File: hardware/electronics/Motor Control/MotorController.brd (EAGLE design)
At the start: 58.4 x 53.3 mm, 10 parts, among them J1 AVR_SPI_PRG_6PTH, U1 ARDUINOR3-BPLACE, U2 ATMEGA328P_TQFP, U3 V_REG_317SMD, X1 HEADER_POS3_70555

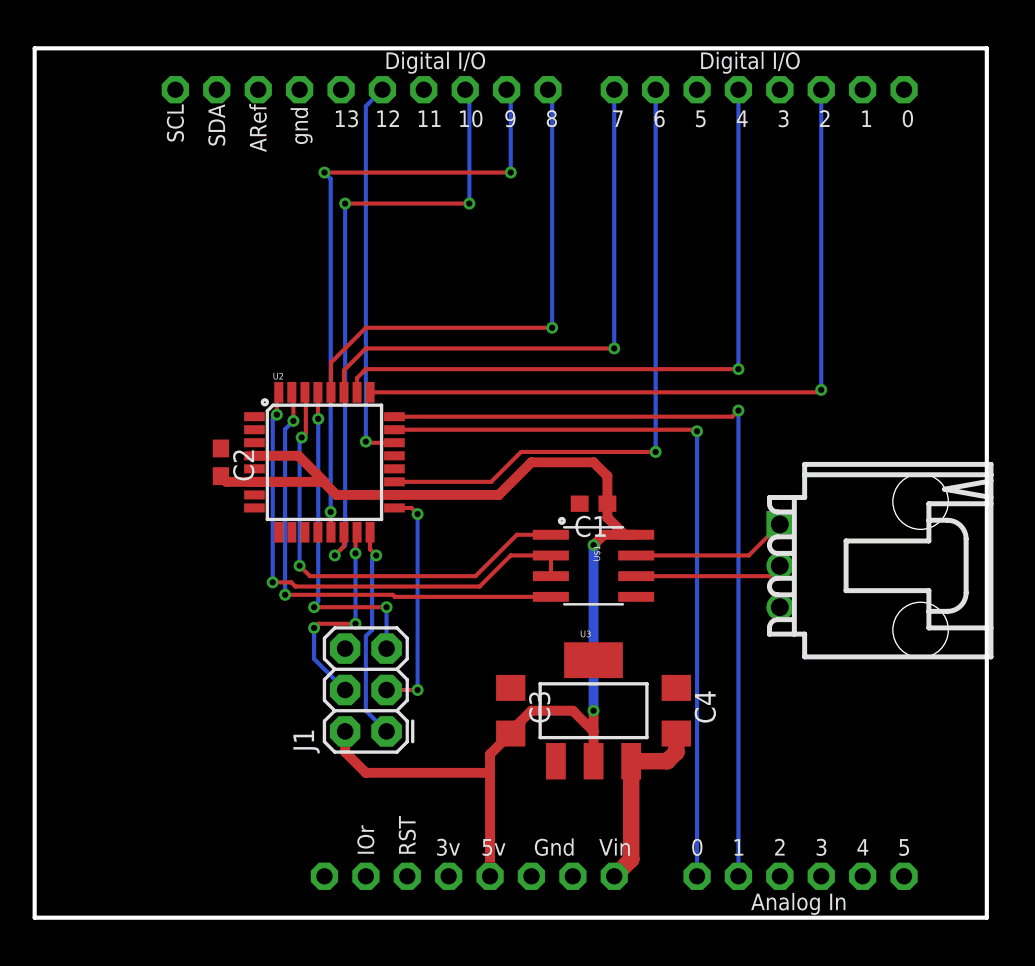
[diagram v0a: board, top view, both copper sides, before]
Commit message: Making sure we have the latest board in github
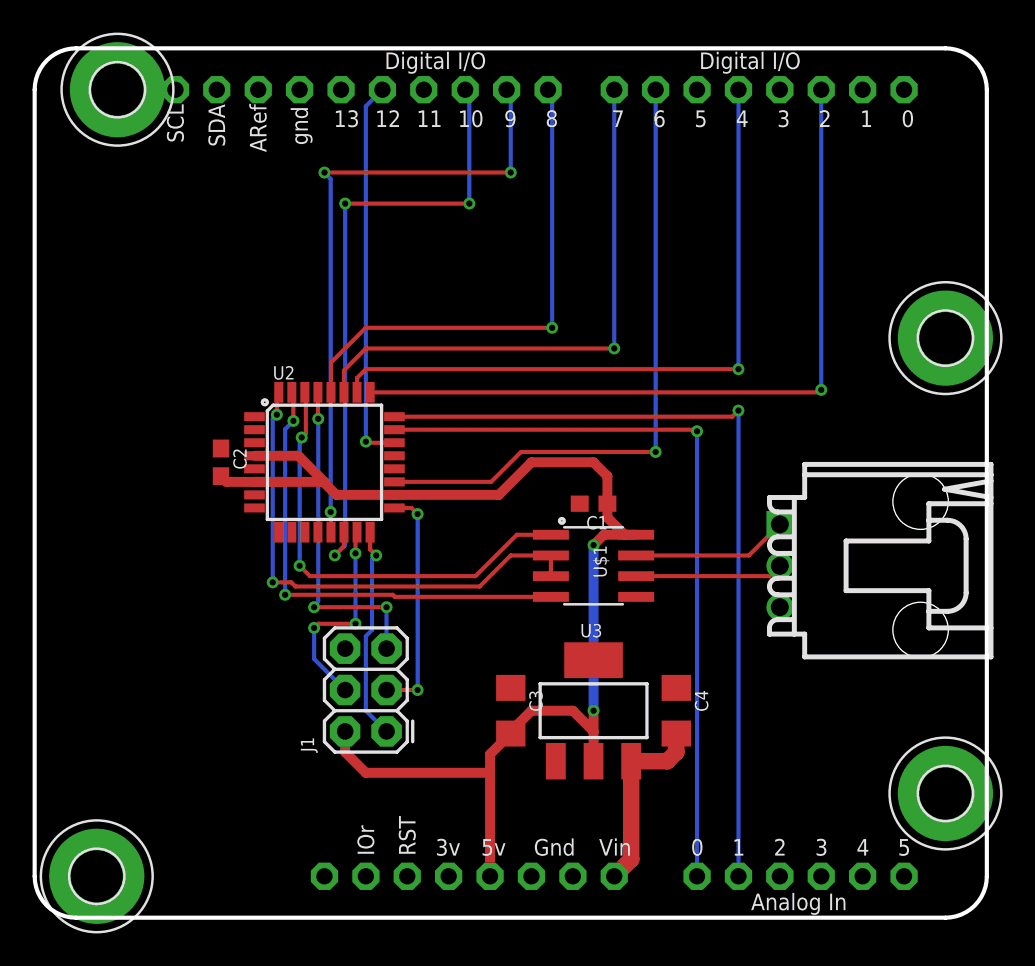
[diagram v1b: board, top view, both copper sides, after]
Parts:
- added H1, H2, H3, H4: MOUNT-PAD-ROUND3.2, holes:3,2-PAD
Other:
- outline, holes or cut-outs redrawn
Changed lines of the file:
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@@
 <board>
 <plain>
-<wire x1="0" y1="0" x2="58.42" y2="0" width="0.254" layer="20"/>
-<wire x1="58.42" y1="0" x2="58.42" y2="53.34" width="0.254" layer="20"/>
-<wire x1="58.42" y1="53.34" x2="0" y2="53.34" width="0.254" layer="20"/>
-<wire x1="0" y1="53.34" x2="0" y2="0" width="0.254" layer="20"/>
+<wire x1="0" y1="50.8" x2="0" y2="2.54" width="0.254" layer="20"/>
+<wire x1="0" y1="2.54" x2="2.54" y2="0" width="0.254" layer="20" curve="90"/>
+<wire x1="2.54" y1="0" x2="55.88" y2="0" width="0.254" layer="20"/>
+<wire x1="55.88" y1="0" x2="58.42" y2="2.54" width="0.254" layer="20" curve="90"/>
+<wire x1="58.42" y1="2.54" x2="58.42" y2="50.8" width="0.254" layer="20"/>
+<wire x1="58.42" y1="50.8" x2="55.88" y2="53.34" width="0.254" layer="20" curve="90"/>
+<wire x1="55.88" y1="53.34" x2="2.54" y2="53.34" width="0.254" layer="20"/>
+<wire x1="2.54" y1="53.34" x2="0" y2="50.8" width="0.254" layer="20" curve="90"/>
 </plain>
 <attributes>
@@
 </autorouter>
 <elements>
-<element name="U1" library="adafruit" package="ARDUINOR3-BPLACE" value="ARDUINOR3-BPLACE" x="-10.16" y="0"/>
-<element name="U$1" library="SparkFun-DigitalIC" package="SO08" value="RS485SOIC" x="34.29" y="21.59" rot="R270"/>
-<element name="J1" library="SparkFun-Connectors" package="2X3" value="AVR_SPI_PRG_6PTH" x="21.59" y="11.43" rot="R90"/>
-<element name="U2" library="SparkFun-DigitalIC" package="TQFP32-08" value="ATMEGA328P_TQFP" x="17.78" y="27.94">
+<element name="U1" library="adafruit" package="ARDUINOR3-BPLACE" value="ARDUINOR3-BPLACE" x="-10.16" y="0" smashed="yes"/>
+<element name="U$1" library="SparkFun-DigitalIC" package="SO08" value="RS485SOIC" x="34.29" y="21.59" smashed="yes" rot="R270">
+<attribute name="VALUE" x="33.655" y="22.86" size="0.8128" layer="27" rot="R270"/>
+<attribute name="NAME" x="34.29" y="22.86" size="0.8128" layer="25" rot="R270"/>
+</element>
+<element name="J1" library="SparkFun-Connectors" package="2X3" value="AVR_SPI_PRG_6PTH" x="21.59" y="11.43" smashed="yes" rot="R90">
+<attribute name="NAME" x="17.145" y="10.16" size="0.8128" layer="25" ratio="10" rot="R90"/>
+<attribute name="VALUE" x="24.765" y="10.16" size="0.8128" layer="27" rot="R90"/>
+</element>
+<element name="U2" library="SparkFun-DigitalIC" package="TQFP32-08" value="ATMEGA328P_TQFP" x="17.78" y="27.94" smashed="yes">
 <attribute name="PROD_ID" value="IC-09069" x="17.78" y="27.94" size="1.778" layer="27" display="off"/>
-</element>
-<element name="U3" library="SparkFun-PowerIC" package="SOT223" value="V_REG_317SMD" x="34.29" y="12.7"/>
-<element name="C1" library="resistor" package="C0603" value="" x="34.29" y="25.4" rot="R180"/>
-<element name="C2" library="resistor" package="C0603" value="" x="11.43" y="27.94" rot="R270"/>
-<element name="C3" library="resistor" package="C1206" value="" x="29.21" y="12.7" rot="R270"/>
-<element name="C4" library="resistor" package="C1206" value="" x="39.37" y="12.7" rot="R270"/>
-<element name="X1" library="con-molex-c-grid-sl" package="70555-POS3" value="HEADER_POS3_70555" x="45.72" y="21.59" rot="R270"/>
+<attribute name="NAME" x="14.605" y="33.02" size="0.8128" layer="25"/>
+<attribute name="VALUE" x="15.24" y="21.59" size="0.8128" layer="27"/>
+</element>
+<element name="U3" library="SparkFun-PowerIC" package="SOT223" value="V_REG_317SMD" x="34.29" y="12.7" smashed="yes">
+<attribute name="NAME" x="33.4645" y="17.2085" size="0.8128" layer="25"/>
+<attribute name="VALUE" x="33.2105" y="12.5095" size="0.8128" layer="27"/>
+</element>
+<element name="C1" library="resistor" package="C0603" value="" x="34.29" y="25.4" smashed="yes" rot="R180">
+<attribute name="NAME" x="35.179" y="24.638" size="0.8128" layer="25" rot="R180"/>
+<attribute name="VALUE" x="35.179" y="27.432" size="1.27" layer="27" rot="R180"/>
+</element>
+<element name="C2" library="resistor" package="C0603" value="" x="11.43" y="27.94" smashed="yes" rot="R270">
+<attribute name="NAME" x="12.192" y="28.829" size="0.8128" layer="25" rot="R270"/>
+<attribute name="VALUE" x="9.398" y="28.829" size="1.27" layer="27" rot="R270"/>
+</element>
+<element name="C3" library="resistor" package="C1206" value="" x="29.21" y="12.7" smashed="yes" rot="R270">
+<attribute name="NAME" x="30.353" y="13.97" size="0.8128" layer="25" rot="R270"/>
+<attribute name="VALUE" x="26.797" y="13.97" size="1.27" layer="27" rot="R270"/>
+</element>
+<element name="C4" library="resistor" package="C1206" value="" x="39.37" y="12.7" smashed="yes" rot="R270">
+<attribute name="NAME" x="40.513" y="13.97" size="0.8128" layer="25" rot="R270"/>
+<attribute name="VALUE" x="36.957" y="13.97" size="1.27" layer="27" rot="R270"/>
+</element>
+<element name="X1" library="con-molex-c-grid-sl" package="70555-POS3" value="HEADER_POS3_70555" x="45.72" y="21.59" smashed="yes" rot="R270"/>
+<element name="H1" library="holes" package="3,2-PAD" value="MOUNT-PAD-ROUND3.2" x="3.81" y="2.54" smashed="yes"/>
+<element name="H2" library="holes" package="3,2-PAD" value="MOUNT-PAD-ROUND3.2" x="55.88" y="7.62" smashed="yes"/>
+<element name="H3" library="holes" package="3,2-PAD" value="MOUNT-PAD-ROUND3.2" x="55.88" y="35.56" smashed="yes"/>
+<element name="H4" library="holes" package="3,2-PAD" value="MOUNT-PAD-ROUND3.2" x="5.08" y="50.8" smashed="yes"/>
 </elements>
 <signals>
@@
 <contactref element="C1" pad="2"/>
 <polygon width="0.254" layer="1" spacing="0.254">
-<vertex x="0" y="0"/>
-<vertex x="58.42" y="0"/>
-<vertex x="58.42" y="53.34"/>
-<vertex x="0" y="53.34"/>
+<vertex x="0" y="50.8"/>
+<vertex x="0" y="2.54" curve="90"/>
+<vertex x="2.54" y="0"/>
+<vertex x="55.88" y="0" curve="90"/>
+<vertex x="58.42" y="2.54"/>
+<vertex x="58.42" y="50.8" curve="90"/>
+<vertex x="55.88" y="53.34"/>
+<vertex x="2.54" y="53.34" curve="90"/>
 </polygon>
 <polygon width="0.254" layer="16" spacing="0.254">
-<vertex x="0" y="0"/>
-<vertex x="58.42" y="0"/>
-<vertex x="58.42" y="53.34"/>
-<vertex x="0" y="53.34"/>
+<vertex x="0" y="50.8"/>
+<vertex x="0" y="2.54" curve="90"/>
+<vertex x="2.54" y="0"/>
+<vertex x="55.88" y="0" curve="90"/>
+<vertex x="58.42" y="2.54"/>
+<vertex x="58.42" y="50.8" curve="90"/>
+<vertex x="55.88" y="53.34"/>
+<vertex x="2.54" y="53.34" curve="90"/>
 </polygon>
 </signal>
